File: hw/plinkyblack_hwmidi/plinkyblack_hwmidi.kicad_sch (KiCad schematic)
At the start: 279 parts, among them J1 AudioJack2_SwitchT, J1 PJ-320B, J10 AudioJack2_SwitchT, J11 AudioJack2_SwitchT, J12 Conn_02x08_Odd_Even, J13 Conn_02x08_Odd_Even, J14 AudioJack2_SwitchT, J15 AudioJack2_SwitchT, J16 AudioJack2_SwitchT, J17 AudioJack2_SwitchT, J18 USB_B_Micro, J19 SJ1-3523N, J2 AudioJack2_SwitchT, J2 PJ-320B, J20 oled0.91, J21 SJ1-3523N, J22 AudioJack2_SwitchT, J23 AudioJack2_SwitchT, J24 USB_B_Micro, J25 Conn_01x16_Female, J26 SJ1-3523N, J27 SJ1-3523N, J3 AudioJack2_SwitchT, J4 AudioJack2_SwitchT, J5 SWD header, J6 AudioJack2_SwitchT, J7 AudioJack2_SwitchT, J8 AudioJack2_SwitchT, J9 AudioJack2_SwitchT, Q1 MMBT3904, U1 HCPL-0631-500E, U1 MCP6002-xSN, U10 TL072, U11 TL072, U12 W25Q32JVSS, U13 TPS61040DBV, U14 W25Q32JVSS, U15 USBLC6-2SC6, U16 TL072, U17 LIS2DH12, U18 TL072, U2 LM1117-3.3, U3 LM1117-3.3, U4 STM32L476VGTx, U5 TL072, U6 WM8758B, U7 TL072, U8 MCP6002-xSN, U9 MCP6002-xSN, Y1 Crystal_GND24

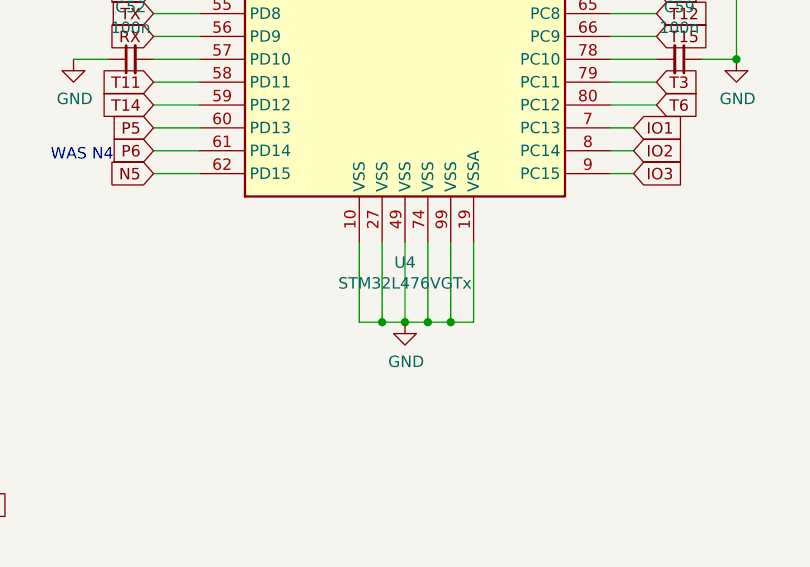
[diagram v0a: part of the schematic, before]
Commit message: update STM chip LCSC part number
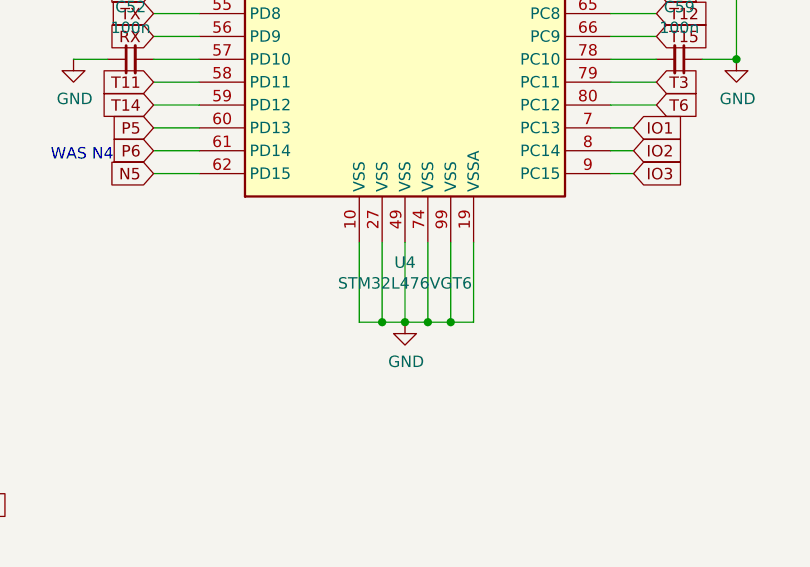
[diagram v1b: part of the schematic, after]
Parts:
- U4: value STM32L476VGTx -> STM32L476VGT6; LCSC C165886 -> C83181
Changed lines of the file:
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@@
       (effects (font (size 1.27 1.27)))
     )
-    (property "Value" "STM32L476VGTx" (at 238.76 310.642 0)
+    (property "Value" "STM32L476VGT6" (at 238.76 310.642 0)
       (effects (font (size 1.27 1.27)))
     )
@@
       (effects (font (size 1.27 1.27)) hide)
     )
-    (property "LCSC" "C165886" (at 238.76 305.7906 0)
+    (property "LCSC" "C83181" (at 238.76 305.7906 0)
       (effects (font (size 1.27 1.27)) hide)
     )
